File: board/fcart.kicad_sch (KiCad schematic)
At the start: 96 parts, among them J1 USB_C_16P, J2 DM3D-SF, J3 JTAG, J4 SWD, J5 Famicom_cartridge, SW1 PTS647SM70, U1 USBLC6-2SC6, U10 W9864G6KH-6, U2 TLV76133DCY, U3 TPS2116, U4 SN74ALVC164245DGG, U5 SN74ALVC164245DGG, U6 SN74ALVC164245DGG, U7 SN74ALVC164245DGG, U8 STM32F412RET6, U9 LCMXO2-4000HC-4TG144, Y1 ABS07-32.768KHZ-7, Y2 ABM8W-12.0000MHZ-8-B1U

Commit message: optimize for native board
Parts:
- added D3: LTST-S326KGJRKT, LED_SMD:LED_LiteOn_LTST-S326, symbol Device:LED_Dual_KAK
- added J6: MSD-4-A, fcart:microSD_HC_Same_Sky_MSD-4-A, symbol Connector:Micro_SD_Card_Det1
- added J8: USB4085, Connector_USB:USB_C_Receptacle_GCT_USB4085, symbol Connector:USB_C_Receptacle_USB2.0_16P
- J1: value USB_C_16P -> USB_C_14P; symbol Connector:USB_C_Receptacle_USB2.0_16P -> Connector:USB_C_Receptacle_USB2.0_14P
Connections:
- net +3V3: now also D3.2 (A)
- net GND: now also J8.A1 (GND), J8.A12 (GND), J8.B1 (GND), J8.B12 (GND), J8.S1 (SHIELD)
- net VUSB: now also J8.A4 (VBUS), J8.A9 (VBUS), J8.B4 (VBUS), J8.B9 (VBUS)
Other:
- note added: "Not needed"
- note added: "locate led under sd"
- note added: "mixed up with cpu_a1 cpu_a2"
- note added: "qspi_clk and ppu_d0 are mixed up"

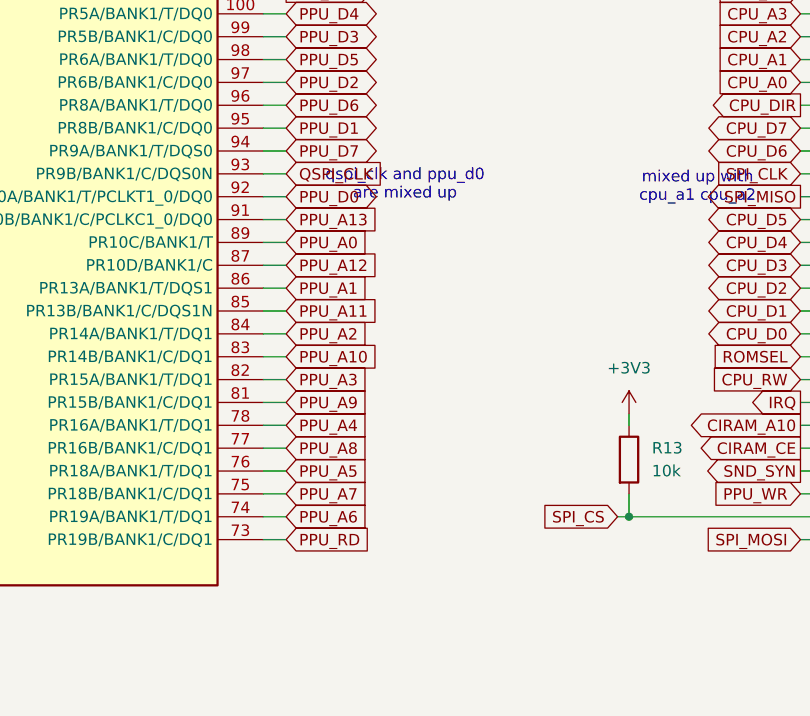
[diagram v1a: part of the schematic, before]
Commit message: loading roms from sdram
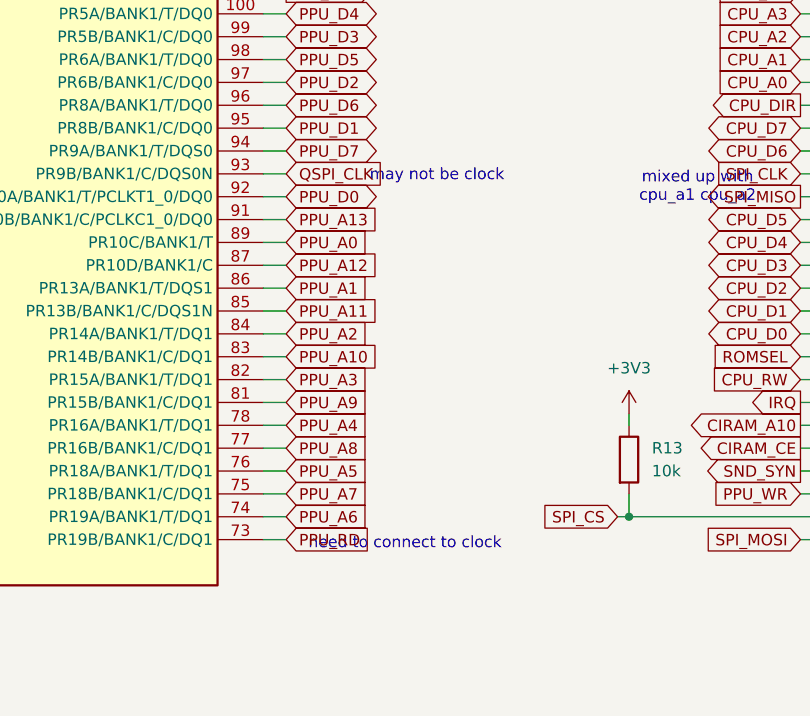
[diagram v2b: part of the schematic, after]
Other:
- note added: "may not be clock"
- note added: "need to connect to clock"
- note removed: "qspi_clk and ppu_d0 are mixed up"
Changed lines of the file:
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@@
 		)
 	)
-	(text "qspi_clk and ppu_d0\nare mixed up"
+	(text "may not be clock"
 		(exclude_from_sim no)
-		(at 168.148 289.56 0)
+		(at 171.704 288.544 0)
 		(effects
 			(font
@@
 		(effects
 			(font
+				(size 1.27 1.27)
+			)
+		)
+	)
+	(text "need to connect to clock"
+		(exclude_from_sim no)
+		(at 168.148 329.438 0)
+		(effects
+			(font

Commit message: Switch to fpga MAX10
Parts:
- removed C25, C32, C33, C34, C35, C36, C37, C47, C48, C49, C50: 0.1u, Capacitor_SMD:C_0805_2012Metric, symbol Device:C
- removed D3: LTST-S326KGJRKT, LED_SMD:LED_LiteOn_LTST-S326, symbol Device:LED_Dual_KAK
- removed J1: USB_C_14P, Connector_USB:USB_C_Receptacle_HRO_TYPE-C-31-M-12, symbol Connector:USB_C_Receptacle_USB2.0_14P
- removed J2: DM3D-SF, Connector_Card:microSD_HC_Hirose_DM3D-SF, symbol Connector:Micro_SD_Card_Det2
- removed R12, R7: 10k, Resistor_SMD:R_0805_2012Metric, symbol Device:R
- removed U9: LCMXO2-4000HC-4TG144, Package_QFP:TQFP-144_20x20mm_P0.5mm, symbol Gekkio_FPGA_Lattice:LCMXO2-4000xx-xTG144
- added C28, C41: 0.1u, Capacitor_SMD:C_0805_2012Metric, symbol Device:C
- added R14, R15: 10k, Resistor_SMD:R_0805_2012Metric, symbol Device:R
- added U9: 10M04SCE144C8G, Package_QFP:EQFP-144-1EP_20x20mm_P0.5mm_EP5x5mm, symbol Gekkio_FPGA_Intel:10M04SCE144
- D1: value LED 3mm -> LTST-S321KRKT; footprint LED_THT:LED_D3.0mm_Horizontal_O1.27mm_Z2.0mm -> fcart:LED_1208_Horizontal_3210Metric
- renumbered C26 to C21, C27 to C22, C21 to C23, C22 to C24, C28 to C25, C23 to C26, C24 to C27, C41 to C32, C42 to C33, C43 to C34, C44 to C35, C45 to C36, C46 to C37, C7 to C6, C6 to C7, J8 to J1, J6 to J2, R9 to R10, R10 to R11, R11 to R12, R8 to R9
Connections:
- net QSPI_CS is gone; now on net SD_DAT3: U8.52 (PC11)
- net QSPI_IO0 is gone; now on net SPI_MISO: U8.22 (PA6)
- net QSPI_IO1 is gone; now on net SPI_MOSI: U8.23 (PA7)
- net SDRAM_UDQM is gone; now on net SDRAM_DQM: U10.39 (UDQM)
- net SPI_CLK is gone; now on net TCK: U8.29 (PB10)
- net +3V3: now also J2.4 (VDD), C28.1, C41.1, R14.1, R15.1, U9.1 (VCC_ONE), U9.103 (VCCIO6), U9.107 (VCCA3), U9.108 (VCC_ONE), U9.109 (VCC_ONE), U9.115 (VCC_ONE), U9.117 (VCCIO7), U9.128 (VCCIO8), U9.139 (VCCIO8), U9.143 (VCCA4), U9.144 (VCC_ONE), U9.2 (VCCA6), U9.23 (VCCIO1B), U9.31 (VCCIO2), U9.34 (VCCA2), U9.35 (VCCA1), U9.36 (VCC_ONE), U9.37 (VCC_ONE), U9.40 (VCCIO3), U9.49 (VCCIO3), U9.5 (VCCA3), U9.51 (VCC_ONE), U9.67 (VCCIO4), U9.71 (VCCA5), U9.72 (VCC_ONE), U9.73 (VCC_ONE), U9.82 (VCCIO5), U9.9 (VCCIO1A), U9.94 (VCCIO6)
- net CIRAM_A10: now also U9.69 (IO4/DIFFIO_TX_RX_B27n/DIFFOUT_B27n)
- net CIRAM_CE: now also U9.70 (IO4/DIFFIO_TX_RX_B27p/DIFFOUT_B27p)
- net CPU_A0: now also U9.52 (IO3/DIFFIO_TX_RX_B9p/DIFFOUT_B9p)
- net CPU_A1: now also U9.50 (IO3/DIFFIO_TX_RX_B9n/DIFFOUT_B9n)
- net CPU_A10: now also U9.30 (IO2/VREFB2N0)
- net CPU_A11: now also U9.28 (IO2/DIFFIO_RX_L20n/DIFFOUT_L20n/CLK1n)
- net CPU_A12: now also U9.29 (IO2/DIFFIO_RX_L20p/DIFFOUT_L20p/CLK1p)
- net CPU_A13: now also U9.32 (IO2/DIFFIO_RX_L27n/DIFFOUT_L27n/PLL_L_CLKOUTn)
- net CPU_A14: now also U9.39 (IO3/DIFFIO_TX_RX_B1p/DIFFOUT_B1p)
- net CPU_A2: now also U9.48 (IO3/VREFB3N0)
- net CPU_A3: now also U9.47 (IO3/DIFFIO_TX_RX_B7p/DIFFOUT_B7p)
- net CPU_A4: now also U9.46 (IO3/DIFFIO_TX_RX_B7n/DIFFOUT_B7n)
- net CPU_A5: now also U9.45 (IO3/DIFFIO_TX_RX_B5p/DIFFOUT_B5p)
- net CPU_A6: now also U9.44 (IO3/DIFFIO_TX_RX_B5n/DIFFOUT_B5n)
- net CPU_A7: now also U9.43 (IO3/DIFFIO_TX_RX_B3p/DIFFOUT_B3p)
- net CPU_A8: now also U9.41 (IO3/DIFFIO_TX_RX_B3n/DIFFOUT_B3n)
- net CPU_A9: now also U9.38 (IO3/DIFFIO_TX_RX_B1n/DIFFOUT_B1n)
- net CPU_D0: now also U9.62 (IO4)
- net CPU_D1: now also U9.61 (IO4/VREFB4N0)
- net CPU_D2: now also U9.60 (IO3/DIFFIO_TX_RX_B16p/DIFFOUT_B16p)
- net CPU_D3: now also U9.59 (IO3/DIFFIO_TX_RX_B16n/DIFFOUT_B16n)
- net CPU_D4: now also U9.58 (IO3/DIFFIO_TX_RX_B14p/DIFFOUT_B14p)
- net CPU_D5: now also U9.57 (IO3/DIFFIO_TX_RX_B14n/DIFFOUT_B14n)
- net CPU_D6: now also U9.56 (IO3/DIFFIO_TX_RX_B12p/DIFFOUT_B12p)
- net CPU_D7: now also U9.55 (IO3/DIFFIO_TX_RX_B12n/DIFFOUT_B12n)
- net CPU_DIR: now also U9.54 (IO3)
- net CPU_RW: now also U9.65 (IO4/DIFFIO_TX_RX_B23p/DIFFOUT_B23p)
- net FPGA_CLK: now also U9.26 (IO2/DIFFIO_RX_L18n/DIFFOUT_L18n/CLK0n)
- net GND: now also J2.10 (SHIELD), J2.6 (VSS), C28.2, C41.2, U9.104 (GND), U9.116 (GND), U9.125 (GND), U9.133 (GND), U9.137 (GND), U9.142 (GND), U9.145 (GND), U9.3 (GND), U9.4 (GND), U9.42 (GND), U9.53 (GND), U9.63 (GND), U9.68 (GND), U9.83 (GND), U9.95 (GND)
- net IRQ: now also U9.66 (IO4)
- net LED: now also U8.55 (PB3); no longer U8.59 (PB7)
- net M2: now also U9.27 (IO2/DIFFIO_RX_L18p/DIFFOUT_L18p/CLK0p)
- net PPU_A0: now also U9.92 (IO6/DIFFIO_RX_R18p/DIFFOUT_R18p)
- net PPU_A1: now also U9.90 (IO6/DIFFIO_RX_R16p/DIFFOUT_R16p/CLK3p)
- net PPU_A10: now also U9.86 (IO5/DIFFIO_RX_R11n/DIFFOUT_R11n)
- net PPU_A11: now also U9.89 (IO6/DIFFIO_RX_R14n/DIFFOUT_R14n/CLK2n)
- net PPU_A12: now also U9.91 (IO6/DIFFIO_RX_R16n/DIFFOUT_R16n/CLK3n)
- net PPU_A13: now also U9.93 (IO6/DIFFIO_RX_R18n/DIFFOUT_R18n)
- net PPU_A2: now also U9.87 (IO5/DIFFIO_RX_R10n/DIFFOUT_R10n)
- net PPU_A3: now also U9.85 (IO5/DIFFIO_RX_R10p/DIFFOUT_R10p)
- net PPU_A4: now also U9.81 (IO5/DIFFIO_RX_R7n/DIFFOUT_R7n)
- net PPU_A5: now also U9.79 (IO5/DIFFIO_RX_R7p/DIFFOUT_R7p)
- net PPU_A6: now also U9.77 (IO5/DIFFIO_RX_R1n/DIFFOUT_R1n)
- net PPU_A7: now also U9.78 (IO5)
- net PPU_A8: now also U9.80 (IO5/VREFB5N0)
- net PPU_A9: now also U9.84 (IO5/DIFFIO_RX_R11p/DIFFOUT_R11p)
- net PPU_D0: now also U9.96 (IO6/DIFFIO_RX_R26p/DIFFOUT_R26p/DPCLK3)
- net PPU_D1: now also U9.98 (IO6/DIFFIO_RX_R26n/DIFFOUT_R26n/DPCLK2)
- net PPU_D2: now also U9.100 (IO6/DIFFIO_RX_R28p/DIFFOUT_R28p)
- net PPU_D3: now also U9.102 (IO6/DIFFIO_RX_R28n/DIFFOUT_R28n)
- net PPU_D4: now also U9.105 (IO6/DIFFIO_RX_R33p/DIFFOUT_R33p)
- net PPU_D5: now also U9.101 (IO6/DIFFIO_RX_R27n/DIFFOUT_R27n)
- net PPU_D6: now also U9.99 (IO6/DIFFIO_RX_R27p/DIFFOUT_R27p)
- net PPU_D7: now also U9.97 (IO6/VREFB6N0)
- net PPU_DIR: now also U9.106 (IO6/DIFFIO_RX_R33n/DIFFOUT_R33n)
- net PPU_RD: now also U9.76 (IO5/DIFFIO_RX_R2n/DIFFOUT_R2n)
- net PPU_WR: now also U9.75 (IO5/DIFFIO_RX_R1p/DIFFOUT_R1p)
- net ROMSEL: now also U9.64 (IO4/DIFFIO_TX_RX_B23n/DIFFOUT_B23n)
- net SDRAM_A0: now also U9.126 (IO8/CONFIG_SEL)
- net SDRAM_A1: now also U9.124 (IO8/DIFFIO_RX_T19p/DIFFOUT_T19p)
- net SDRAM_A10: now also U9.127 (IO8/DIFFIO_RX_T19n/DIFFOUT_T19n)
- net SDRAM_A11: now also U9.112 (IO7/VREFB7N0)
- net SDRAM_A2: now also U9.123 (IO8/VREFB8N0)
- net SDRAM_A3: now also U9.122 (IO8/DEV_OE)
- net SDRAM_A4: now also U9.121 (IO8/DIFFIO_RX_T16n/DIFFOUT_T16n/DEV_CLRn)
- net SDRAM_A5: now also U9.120 (IO8/DIFFIO_RX_T16p/DIFFOUT_T16p)
- net SDRAM_A6: now also U9.119 (IO7/DIFFIO_RX_T10n/DIFFOUT_T10n)
- net SDRAM_A7: now also U9.118 (IO7/DIFFIO_RX_T10p/DIFFOUT_T10p)
- net SDRAM_A8: now also U9.114 (IO7)
- net SDRAM_A9: now also U9.113 (IO7)
- net SDRAM_BA0: now also U9.131 (IO8/DIFFIO_RX_T20n/DIFFOUT_T20n)
- net SDRAM_BA1: now also U9.130 (IO8/DIFFIO_RX_T20p/DIFFOUT_T20p)
- net SDRAM_CAS: now also U9.135 (IO8)
- net SDRAM_CLK: now also U9.33 (IO2/DIFFIO_RX_L27p/DIFFOUT_L27p/PLL_L_CLKOUTp)
- net SDRAM_CS: now also U9.132 (IO8/DIFFIO_RX_T22p/DIFFOUT_T22p)
- net SDRAM_DQ0: now also U9.25 (IO1B/DIFFIO_RX_L16p/DIFFOUT_L16p)
- net SDRAM_DQ1: now also U9.24 (IO1B/DIFFIO_RX_L16n/DIFFOUT_L16n)
- net SDRAM_DQ10: now also U9.6 (IO1A/DIFFIO_RX_L1n/DIFFOUT_L1n)
- net SDRAM_DQ11: now also U9.7 (IO1A/DIFFIO_RX_L1p/DIFFOUT_L1p)
- net SDRAM_DQ12: now also U9.8 (IO1A/DIFFIO_RX_L3n/DIFFOUT_L3n)
- net SDRAM_DQ13: now also U9.10 (IO1A/DIFFIO_RX_L3p/DIFFOUT_L3p)
- net SDRAM_DQ14: now also U9.11 (IO1A/DIFFIO_RX_L5n/DIFFOUT_L5n)
- net SDRAM_DQ15: now also U9.12 (IO1A/DIFFIO_RX_L5p/DIFFOUT_L5p)
- net SDRAM_DQ2: now also U9.22 (IO1B/DIFFIO_RX_L14p/DIFFOUT_L14p)
- net SDRAM_DQ3: now also U9.21 (IO1B/DIFFIO_RX_L14n/DIFFOUT_L14n)
- net SDRAM_DQ4: now also U9.13 (IO1A/DIFFIO_RX_L7n/DIFFOUT_L7n)
- net SDRAM_DQ5: now also U9.14 (IO1A/DIFFIO_RX_L7p/DIFFOUT_L7p)
- net SDRAM_DQ6: now also U9.15 (IO1B/JTAGEN)
- net SDRAM_DQ7: now also U9.17 (IO1B/VREFB1N0)
- net SDRAM_DQ8: now also U9.141 (IO8/DIFFIO_RX_T26n/DIFFOUT_T26n)
- net SDRAM_DQ9: now also U9.140 (IO8/DIFFIO_RX_T26p/DIFFOUT_T26p)
- net SDRAM_RAS: now also U9.134 (IO8/DIFFIO_RX_T22n/DIFFOUT_T22n/CRC_ERROR)
- net SDRAM_WE: now also R15.2, U9.136 (IO8/DIFFIO_RX_T24p/DIFFOUT_T24p/nSTATUS)
- net SD_CLK: now also J2.5 (CLK)
- net SD_CMD: now also J2.3 (CMD)
- net SD_DAT0: now also J2.7 (DAT0)
- net SD_DAT1: now also J2.8 (DAT1)
- net SD_DAT2: now also J2.1 (DAT2), U8.42 (PA9); no longer U8.51 (PC10)
- net SD_DAT3: now also J2.2 (DAT3/CD); no longer U8.57 (PB5)
- net SD_DET: now also J2.9 (DET), U8.51 (PC10); no longer U8.58 (PB6)
- net SND_SYN: now also U9.74 (IO5/DIFFIO_RX_R2p/DIFFOUT_R2p)
- net SPI_CS: now also U8.56 (PB4), U9.129 (IN8/nCONFIG); no longer U8.9 (PC1)
- net SPI_MISO: now also U9.111 (IO7/DIFFIO_RX_T1n/DIFFOUT_T1n); no longer U8.10 (PC2)
- net SPI_MOSI: now also U9.110 (IO7/DIFFIO_RX_T1p/DIFFOUT_T1p); no longer U8.11 (PC3)
- net TCK: now also J3.2 (Pin_2), U9.18 (IO1B/DIFFIO_RX_L11p/DIFFOUT_L11p/TCK); no longer J3.5 (Pin_5)
- net TDI: now also J3.5 (Pin_5), U8.11 (PC3), U9.19 (IO1B/DIFFIO_RX_L12n/DIFFOUT_L12n/TDI); no longer J3.3 (Pin_3)
- net TDO: now also J3.3 (Pin_3), U8.10 (PC2), U9.20 (IO1B/DIFFIO_RX_L12p/DIFFOUT_L12p/TDO); no longer J3.2 (Pin_2)
- net TMS: now also U8.38 (PC7), U9.16 (IO1B/DIFFIO_RX_L11n/DIFFOUT_L11n/TMS)
- net at R2.1: now also J1.B5 (CC2)
- net at J1.A5 (CC1): now also R1.1
- net at J1.A6 (D+): now also J1.B6 (D+), U1.3 (I/O2)
- net at J1.A7 (D-): now also J1.B7 (D-), U1.1 (I/O1)
- net QSPI_CLK: no longer names the net of U8.27 (PB1)
- net QSPI_IO2: no longer names the net of U8.24 (PC4)
- net QSPI_IO3: no longer names the net of U8.25 (PC5)
- net QSPI_IRQ renamed SPI_SCK
- net SPI_SCK: now also U9.88 (IO6/DIFFIO_RX_R14p/DIFFOUT_R14p/CLK2p)
- net SDRAM_LDQM renamed SDRAM_DQM
- net SDRAM_DQM: now also R14.2, U9.138 (IO8/DIFFIO_RX_T24n/DIFFOUT_T24n/CONF_DONE)
- no-connect marks 43 -> 42
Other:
- note added: "place near SD"
- note removed: "Not needed"
- note removed: "locate led under sd"
- note removed: "may not be clock"
- note removed: "mixed up with cpu_a1 cpu_a2"
- note removed: "need to connect to clock"
- moved on the sheet: C6, C7, J1, J2, J3, R12, R9

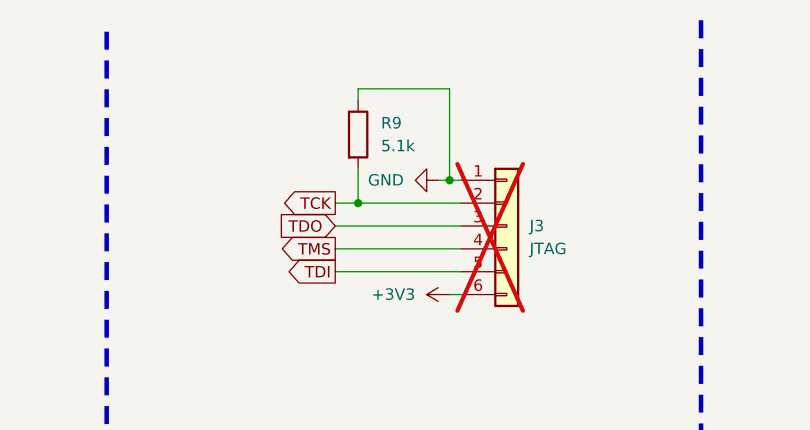
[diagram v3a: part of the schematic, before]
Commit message: switch mcu to max 10 board
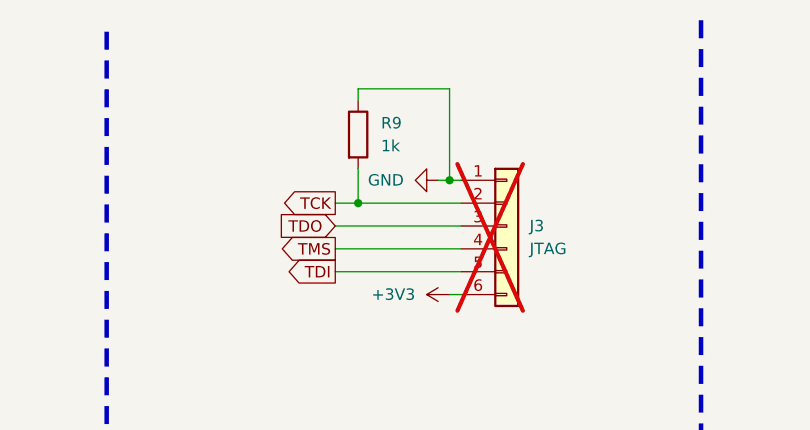
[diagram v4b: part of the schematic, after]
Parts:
- R9: value 5.1k -> 1k
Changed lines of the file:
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@@
 			)
 		)
-		(property "Value" "5.1k"
+		(property "Value" "1k"
 			(at 383.54 26.6699 0)
 			(effects

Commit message: New board design based on MachXO2
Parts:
- removed R14, R15: 10k, Resistor_SMD:R_0805_2012Metric, symbol Device:R
- removed U9: 10M04SCE144C8G, Package_QFP:EQFP-144-1EP_20x20mm_P0.5mm_EP5x5mm, symbol Gekkio_FPGA_Intel:10M04SCE144
- added C29, C32, C33, C34, C35, C36, C38, C39, C46: 0.1u, Capacitor_SMD:C_0805_2012Metric, symbol Device:C
- added U10: LCMXO2-4000HC-4TG144C, Package_QFP:TQFP-144_20x20mm_P0.5mm, symbol Gekkio_FPGA_Lattice:LCMXO2-4000xx-xTG144
- added Y3: ASE-50.000MHZ-LC, Oscillator:Oscillator_SMD_Abracon_ASE-4Pin_3.2x2.5mm, symbol Oscillator:ASE-xxxMHz
- R1: renamed from R9; value 1k -> 5.1k
- renumbered C10 to C1, C4 to C10, C5 to C11, C23 to C21, C24 to C22, C26 to C23, C27 to C24, C21 to C25, C22 to C26, C25 to C27, C6 to C3, C29 to C37, C7 to C4, C32 to C40, C33 to C41, C34 to C42, C35 to C43, C36 to C44, C37 to C45, C38 to C47, C39 to C48, C40 to C49, C11 to C5, C41 to C50, C9 to C6, C8 to C7, C1 to C8, C3 to C9, J3 to J1, J1 to J2, J2 to J3, R12 to R10, R13 to R11, R1 to R2, R2 to R4, R4 to R6, R10 to R7, R11 to R8, R6 to R9, U3 to U1, U1 to U2, U2 to U3, U10 to U9
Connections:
- net FPGA_CLK is gone; now on net SD_DAT1: U8.41 (PA8)
- net +3V3: now also C29.1, C32.1, C33.1, C34.1, C35.1, C36.1, C38.1, C39.1, C46.1, U10.102 (VCCIO1), U10.108 (VCC), U10.118 (VCCIO0), U10.123 (VCCIO0), U10.135 (VCCIO0), U10.144 (VCC), U10.16 (VCCIO4), U10.30 (VCCIO3), U10.36 (VCC), U10.37 (VCCIO2), U10.51 (VCCIO2), U10.66 (VCCIO2), U10.7 (VCCIO5), U10.72 (VCC), U10.79 (VCCIO1), U10.88 (VCCIO1), Y3.4 (Vdd)
- net BTN: now also U8.26 (PB0); no longer U8.20 (PA4)
- net CIRAM_A10: now also U10.65 (PB27A/BANK2/T)
- net CIRAM_CE: now also U10.67 (PB27B/BANK2/C)
- net CPU_A0: now also U10.49 (PB13A/BANK2/T/PCLKT2_0)
- net CPU_A1: now also U10.48 (PB10B/BANK2/C)
- net CPU_A10: now also U10.32 (PL19A/BANK3/T)
- net CPU_A11: now also U10.28 (PL17B/BANK3/C/PCLKC3_0)
- net CPU_A12: now also U10.31 (PL18D/BANK3)
- net CPU_A13: now also U10.33 (PL19B/BANK3/C)
- net CPU_A14: now also U10.35 (PL20B/BANK3/C)
- net CPU_A2: now also U10.47 (PB10A/BANK2/T)
- net CPU_A3: now also U10.43 (PB7B/BANK2/C)
- net CPU_A4: now also U10.42 (PB7A/BANK2/T)
- net CPU_A5: now also U10.41 (PB4B/BANK2/C)
- net CPU_A6: now also U10.40 (PB4A/BANK2/T/CSSPIN)
- net CPU_A7: now also U10.39 (PB3B/BANK2/C)
- net CPU_A8: now also U10.38 (PB3A/BANK2/T)
- net CPU_A9: now also U10.34 (PL20A/BANK3/T)
- net CPU_D0: now also U10.60 (PB23B/BANK2/C)
- net CPU_D1: now also U10.59 (PB23A/BANK2/T)
- net CPU_D2: now also U10.58 (PB21B/BANK2/C)
- net CPU_D3: now also U10.57 (PB21A/BANK2/T)
- net CPU_D4: now also U10.56 (PB20B/BANK2/C/PCLKC2_1)
- net CPU_D5: now also U10.55 (PB20A/BANK2/T/PCLKT2_1)
- net CPU_D6: now also U10.54 (PB15B/BANK2/C)
- net CPU_D7: now also U10.52 (PB15A/BANK2/T)
- net CPU_DIR: now also U10.50 (PB13B/BANK2/C/PCLKC2_0)
- net CPU_RW: now also U10.62 (PB24B/BANK2/C)
- net GND: now also R1.2, C29.2, C32.2, C33.2, C34.2, C35.2, C36.2, C38.2, C39.2, C46.2, U10.101 (GND), U10.116 (GND), U10.124 (GND), U10.134 (GND), U10.18 (GND), U10.29 (GND), U10.46 (GND), U10.53 (GND), U10.64 (GND), U10.8 (GND), U10.80 (GND), U10.90 (GND), Y3.2 (GND); no longer R1.1
- net IRQ: now also U10.63 (PB24D/BANK2)
- net LED: now also U8.62 (PB9); no longer U8.55 (PB3)
- net M2: now also U10.27 (PL17A/BANK3/T/PCLKT3_0)
- net PPU_A0: now also U10.89 (PR10C/BANK1/T)
- net PPU_A1: now also U10.86 (PR13A/BANK1/T/DQS1)
- net PPU_A10: now also U10.83 (PR14B/BANK1/C/DQ1)
- net PPU_A11: now also U10.85 (PR13B/BANK1/C/DQS1N)
- net PPU_A12: now also U10.87 (PR10D/BANK1/C)
- net PPU_A13: now also U10.91 (PR10B/BANK1/C/PCLKC1_0/DQ0)
- net PPU_A2: now also U10.84 (PR14A/BANK1/T/DQ1)
- net PPU_A3: now also U10.82 (PR15A/BANK1/T/DQ1)
- net PPU_A4: now also U10.78 (PR16A/BANK1/T/DQ1)
- net PPU_A5: now also U10.76 (PR18A/BANK1/T/DQ1)
- net PPU_A6: now also U10.74 (PR19A/BANK1/T/DQ1)
- net PPU_A7: now also U10.75 (PR18B/BANK1/C/DQ1)
- net PPU_A8: now also U10.77 (PR16B/BANK1/C/DQ1)
- net PPU_A9: now also U10.81 (PR15B/BANK1/C/DQ1)
- net PPU_D0: now also U10.93 (PR9B/BANK1/C/DQS0N)
- net PPU_D1: now also U10.95 (PR8B/BANK1/C/DQ0)
- net PPU_D2: now also U10.97 (PR6B/BANK1/C/DQ0)
- net PPU_D3: now also U10.99 (PR5B/BANK1/C/DQ0)
- net PPU_D4: now also U10.100 (PR5A/BANK1/T/DQ0)
- net PPU_D5: now also U10.98 (PR6A/BANK1/T/DQ0)
- net PPU_D6: now also U10.96 (PR8A/BANK1/T/DQ0)
- net PPU_D7: now also U10.94 (PR9A/BANK1/T/DQS0)
- net PPU_DIR: now also U10.103 (PR4C/BANK1)
- net PPU_RD: now also U10.73 (PR19B/BANK1/C/DQ1)
- net PPU_WR: now also U10.69 (PB29B/BANK2/C)
- net ROMSEL: now also U10.61 (PB24A/BANK2/T)
- net SDRAM_A0: now also U10.140 (PT10B/BANK0/C/LVDS)
- net SDRAM_A1: now also U10.139 (PT11A/BANK0/T/LVDS)
- net SDRAM_A10: now also U10.141 (PT10A/BANK0/T/LVDS)
- net SDRAM_A11: now also U10.120 (PT23C/BANK0/T/JTAGENB)
- net SDRAM_A2: now also U10.138 (PT11B/BANK0/C/LVDS)
- net SDRAM_A3: now also U10.133 (PT14A/BANK0/T/LVDS)
- net SDRAM_A4: now also U10.132 (PT14B/BANK0/C/LVDS)
- net SDRAM_A5: now also U10.127 (PT18B/BANK0/C/PCLKC0_1/LVDS)
- net SDRAM_A6: now also U10.126 (PT20C/BANK0/T/SCL/PCLKT0_0)
- net SDRAM_A7: now also U10.125 (PT20D/BANK0/C/SDA/PCLKC0_0)
- net SDRAM_A8: now also U10.122 (PT21A/BANK0/T/LVDS)
- net SDRAM_A9: now also U10.121 (PT21B/BANK0/C/LVDS)
- net SDRAM_BA0: now also U10.143 (PT9A/BANK0/T/LVDS)
- net SDRAM_BA1: now also U10.142 (PT9B/BANK0/C/LVDS)
- net SDRAM_CAS: now also U10.24 (PL14B/BANK4/C)
- net SDRAM_CLK: now also U10.128 (PT18A/BANK0/T/PCLKT0_1/LVDS)
- net SDRAM_CS: now also U10.22 (PL13B/BANK4/C)
- net SDRAM_DQ0: now also U10.12 (PL8B/BANK5/C)
- net SDRAM_DQ1: now also U10.13 (PL9A/BANK4/T)
- net SDRAM_DQ10: now also U10.4 (PL4B/BANK5/C/L_GPLLC_IN)
- net SDRAM_DQ11: now also U10.5 (PL6A/BANK5/T/PCLKT5_0)
- net SDRAM_DQ12: now also U10.6 (PL6B/BANK5/C/PCLKC5_0)
- net SDRAM_DQ13: now also U10.9 (PL7A/BANK5/T)
- net SDRAM_DQ14: now also U10.10 (PL7B/BANK5/C)
- net SDRAM_DQ15: now also U10.11 (PL8A/BANK5/T)
- net SDRAM_DQ2: now also U10.14 (PL9B/BANK4/C)
- net SDRAM_DQ3: now also U10.15 (PL10A/BANK4/T)
- net SDRAM_DQ4: now also U10.17 (PL10B/BANK4/C)
- net SDRAM_DQ5: now also U10.19 (PL10C/BANK4/T/PCLKT4_0)
- net SDRAM_DQ6: now also U10.20 (PL10D/BANK4/C/PCLKC4_0)
- net SDRAM_DQ7: now also U10.21 (PL13A/BANK4/T)
- net SDRAM_DQ8: now also U10.2 (PL3B/BANK5/C/L_GPLLC_FB)
- net SDRAM_DQ9: now also U10.3 (PL4A/BANK5/T/L_GPLLT_IN)
- net SDRAM_RAS: now also U10.23 (PL14A/BANK4/T)
- net SDRAM_WE: now also U10.25 (PL16A/BANK3/T)
- net SD_DAT0: now also U8.56 (PB4); no longer U8.39 (PC8)
- net SD_DAT1: no longer U8.40 (PC9)
- net SD_DAT3: now also U8.57 (PB5); no longer U8.52 (PC11)
- net SD_DET: now also U8.50 (PA15); no longer U8.51 (PC10)
- net SND_SYN: now also U10.68 (PB29A/BANK2/T)
- net SPI_MISO: now also U10.45 (PB9B/BANK2/C/SO/SPISO)
- net SPI_MOSI: now also U10.71 (PB30B/BANK2/C/SI/SISPI)
- net SPI_SCK: now also U10.44 (PB9A/BANK2/T/MCLK/CCLK)
- net SWCLK: now also J4.2 (Pin_2); no longer J4.3 (Pin_3)
- net SWDIO: now also J4.3 (Pin_3); no longer J4.2 (Pin_2)
- net TCK: now also J1.4 (Pin_4), R1.1, U10.131 (PT15C/BANK0/T/TCK); no longer J1.2 (Pin_2), R1.2, U8.29 (PB10)
- net TDI: now also J1.3 (Pin_3), U10.136 (PT13D/BANK0/C/TDI); no longer J1.5 (Pin_5), U8.11 (PC3)
- net TDO: now also J1.2 (Pin_2), U10.137 (PT13C/BANK0/T/TDO); no longer J1.3 (Pin_3), U8.10 (PC2)
- net TMS: now also J1.5 (Pin_5), U10.130 (PT15D/BANK0/C/TMS); no longer J1.4 (Pin_4), U8.38 (PC7)
- net QSPI_IO3: now reaches U8.15 (PA1)
- net QSPI_IO3: now also U10.114 (PT25A/BANK0/T/LVDS)
- net SPI_NCS: now reaches U8.24 (PC4)
- net SPI_NCS: now also R11.2, U10.70 (PB30A/BANK2/T/SN)
- net QSPI_CLK: now reaches U8.27 (PB1)
- net QSPI_CLK: now also U10.92 (PR10A/BANK1/T/PCLKT1_0/DQ0)
- net QSPI_NCS: now reaches U8.58 (PB6)
- net QSPI_NCS: now also U10.115 (PT24B/BANK0/C/LVDS)
- net FPGA_IRQ: now reaches U8.59 (PB7)
- net FPGA_IRQ: now also U10.117 (PT24A/BANK0/T/LVDS)
- net SDRAM_DQM renamed SDRAM_LDQM
- net SDRAM_LDQM: now also U10.26 (PL16B/BANK3/C); no longer U9.39 (UDQM)
- removed net SPI_CS: R11.2, U8.56 (PB4)
- new net: U10.105 (PR3A/BANK1/T/R_GPLLT_IN/DQ0), Y3.3 (OUT)
- new net QSPI_IO0: U10.112 (PT27A/BANK0/T/LVDS), U8.40 (PC9)
- new net QSPI_IO1: U10.113 (PT25B/BANK0/C/LVDS), U8.51 (PC10)
- new net QSPI_IO2: U10.111 (PT27B/BANK0/C/LVDS), U8.39 (PC8)
- new net SDRAM_UDQM: U10.1 (PL3A/BANK5/T/L_GPLLT_FB), U9.39 (UDQM)
- no-connect marks 42 -> 47
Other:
- moved on the sheet: C37, C40, C41, C42, C43, C44, C45, C47, C48, C49, C50, R1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
